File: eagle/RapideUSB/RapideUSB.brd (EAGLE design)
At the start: 50 x 50 mm, 37 parts, among them Y1 12-20MHz

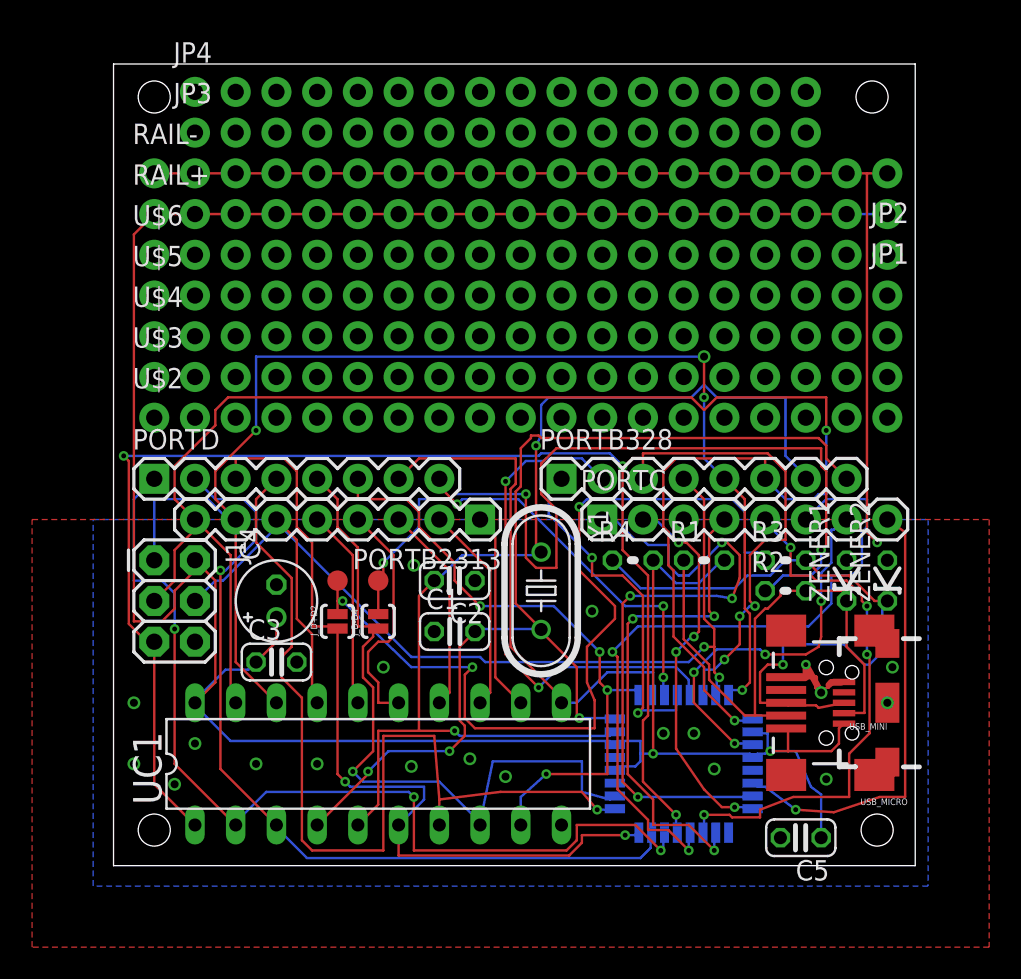
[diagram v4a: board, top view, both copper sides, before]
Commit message: Lots of improvements
Moved vias further from the mCU, changes to comply to the most recent
DRC of Seeedstudio. This board GND plane is a nightmare, maybe doing
more bad than good...
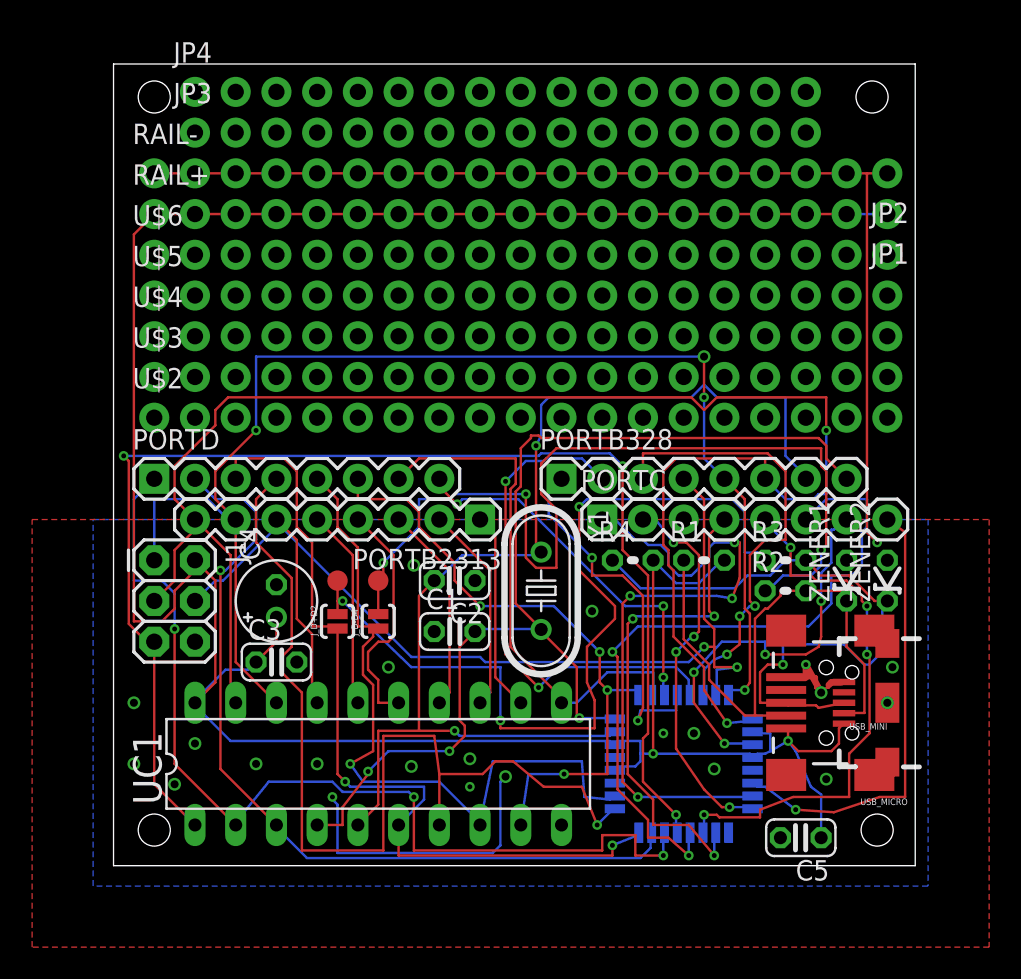
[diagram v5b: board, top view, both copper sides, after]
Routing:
- net GND: track 76.1 -> 94.5 mm, vias 21 -> 23
- net D3: track 57.5 -> 60.3 mm
- net MOSI: track 65.7 -> 68.0 mm
- net D0: track 59.8 -> 61.2 mm
- net N$11: track 24.1 -> 25.2 mm
- net VCC: track 171.3 -> 170.4 mm
- net B0: track 22.6 -> 23.4 mm
- net B7: track 66.0 -> 66.8 mm
- net N$10: track 43.6 -> 44.3 mm
- net N$5: track 41.4 -> 42.0 mm
- net N$8: track 31.0 -> 31.5 mm

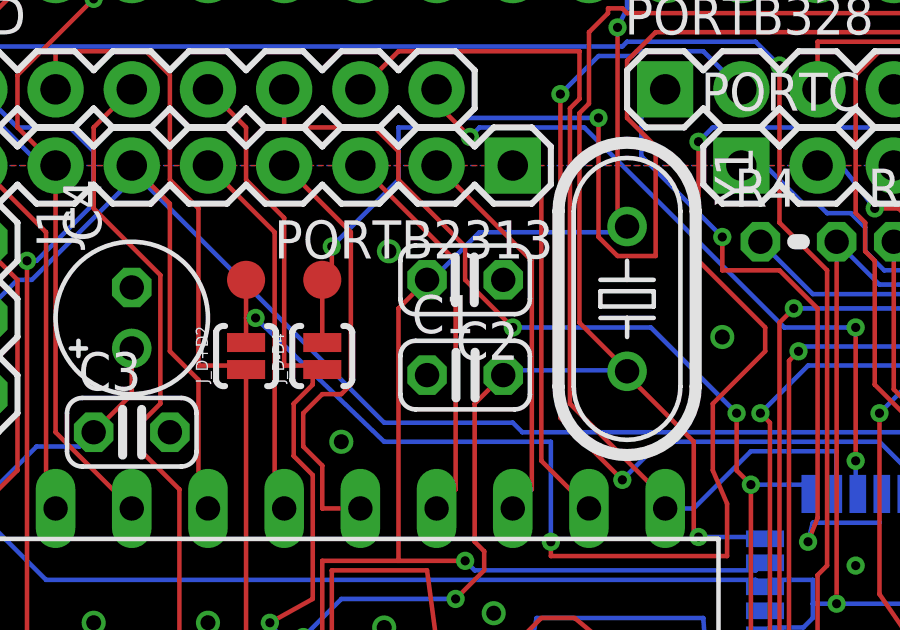
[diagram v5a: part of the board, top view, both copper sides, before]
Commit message: Added 2 alternate SMD 22pF caps
That makes 2 airwire because I can't attach to the pad center, but once
made the connection should be all ok.
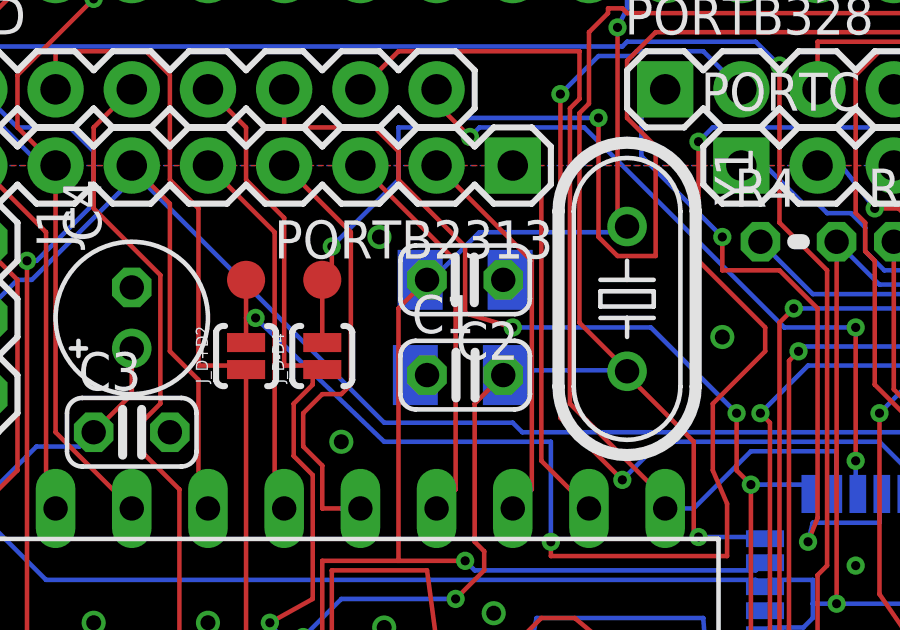
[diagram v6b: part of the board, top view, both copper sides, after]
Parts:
- added C6, C7: (no value), resistor:C1206K
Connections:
- net B6: now also C7.2
- net B7: now also C6.2
- net GND: now also C6.1, C7.1
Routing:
- net D5: track 39.6 -> 40.1 mm
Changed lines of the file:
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@@
 <element name="C5" library="resistor" package="C025-024X044" value="1uF" x="42.8625" y="1.74625" rot="R180"/>
 <element name="U$1" library="kalshagar-images" package="VUSB_LOGO" value="" x="32.385" y="12.3825"/>
+<element name="C6" library="resistor" package="C1206K" value="" x="21.11375" y="14.605" rot="MR180"/>
+<element name="C7" library="resistor" package="C1206K" value="" x="21.2725" y="17.78" rot="MR0"/>
 </elements>
 <signals>
@@
 <via x="48.26" y="10.16" extent="1-16" drill="0.5" shape="octagon"/>
 <via x="17.145" y="12.3825" extent="1-16" drill="0.5" shape="octagon"/>
-<via x="18.7325" y="18.7325" extent="1-16" drill="0.5" shape="octagon"/>
+<via x="18.415" y="19.20875" extent="1-16" drill="0.5" shape="octagon"/>
 <via x="24.4475" y="5.55625" extent="1-16" drill="0.5" shape="octagon"/>
 <via x="34.29" y="8.255" extent="1-16" drill="0.3048" shape="octagon"/>
@@
 <wire x1="24.13" y1="5.23875" x2="24.4475" y2="5.55625" width="0.1524" layer="16"/>
 <via x="22.225" y="4.92125" extent="1-16" drill="0.3048"/>
+<contactref element="C6" pad="1"/>
+<contactref element="C7" pad="1"/>
 </signal>
 <signal name="B7">
@@
 <via x="20.955" y="7.14375" extent="1-16" drill="0.3048"/>
 <via x="29.05125" y="9.2075" extent="1-16" drill="0.3048"/>
+<contactref element="C6" pad="2"/>
+<wire x1="22.5425" y1="14.605" x2="22.61375" y2="14.605" width="0" layer="19" extent="16-16"/>
 </signal>
 <signal name="B6">
@@
 <via x="21.2725" y="8.41375" extent="1-16" drill="0.3048"/>
 <via x="26.3525" y="26.19375" extent="1-16" drill="0.3048"/>
+<contactref element="C7" pad="2"/>
+<wire x1="20.0025" y1="17.78" x2="19.84375" y2="17.78" width="0.1524" layer="16"/>
+<wire x1="19.84375" y1="17.78" x2="19.7725" y2="17.78" width="0" layer="19" extent="16-16"/>
 </signal>
 <signal name="RESET">
@@
 <wire x1="27.46375" y1="16.1925" x2="30.32125" y2="13.335" width="0.1524" layer="16"/>
 <wire x1="22.86" y1="16.1925" x2="27.46375" y2="16.1925" width="0.1524" layer="16"/>
-<wire x1="21.2725" y1="17.78" x2="22.86" y2="16.1925" width="0.1524" layer="1"/>
-<wire x1="21.2725" y1="18.89125" x2="21.2725" y2="17.78" width="0.1524" layer="1"/>
+<wire x1="21.2725" y1="16.66875" x2="22.86" y2="16.1925" width="0.1524" layer="1"/>
+<wire x1="21.2725" y1="18.89125" x2="21.2725" y2="16.66875" width="0.1524" layer="1"/>
 <wire x1="19.05" y1="21.11375" x2="21.2725" y2="18.89125" width="0.1524" layer="1"/>
 <wire x1="19.05" y1="22.06625" x2="19.05" y2="21.11375" width="0.1524" layer="1"/>
